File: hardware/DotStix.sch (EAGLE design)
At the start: 22 parts, among them IC1 CAT24M010TS, U1 ATMEGA328P-MU-QFN32, U2 TMP102

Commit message: Add NMOS to minimize leakage through 100uF cap
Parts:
- removed D2: (no value), diode:DIODE-SOD523
- added Q2: BSH103, adafruit:MOSFET-NREFLOW
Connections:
- new net N$5: C6.1, Q2.S
- new net TMP112_VCC: U1.PB6(XTAL1/TOSC1/PCINT6), U2.VCC
- new net VCC_100UF_CAP: Q2.G, U1.PB7(XTAL2/TOSC2/PCINT7)
- net +3V3: now also Q2.D; no longer C6.1, D2.C, U2.VCC
- net GND: no longer D2.A
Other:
- note added: "TMP112 needs VCC from MCU I/O. (reduces draw from 7uA -> ? nA)"
- moved on the sheet: C6, U2
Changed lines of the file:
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@@
 <part name="SUPPLY5" library="supply2" deviceset="GND" device=""/>
 <part name="D1" library="SparkFun" deviceset="SOLAR-IXYS" device="-"/>
-<part name="D2" library="diode" deviceset="DIODE-" device="SOD523"/>
-<part name="SUPPLY8" library="supply2" deviceset="GND" device=""/>
 <part name="D3" library="diode" deviceset="DIODE-" device="SOD523"/>
 <part name="+3V9" library="supply1" deviceset="+3V3" device=""/>
@@
 <part name="U2" library="SparkFun" deviceset="TMP102" device=""/>
 <part name="SUPPLY15" library="supply2" deviceset="GND" device=""/>
-<part name="+3V12" library="supply1" deviceset="+3V3" device=""/>
 <part name="SUPPLY7" library="supply2" deviceset="GND" device=""/>
 <part name="SUPPLY9" library="supply2" deviceset="GND" device=""/>
@@
 <part name="TP5" library="testpad" deviceset="TP" device="TP20SQ"/>
 <part name="TP6" library="testpad" deviceset="TP" device="TP20SQ"/>
+<part name="Q2" library="adafruit" deviceset="MOSFET-N" device="REFLOW" value="BSH103"/>
 </parts>
 <sheets>
@@
 <wire x1="223.52" y1="-5.08" x2="223.52" y2="-86.36" width="0.1524" layer="95" style="longdash"/>
 <text x="167.64" y="-81.28" size="3.81" layer="95">Storage</text>
+<text x="386.08" y="173.99" size="1.27" layer="91">TMP112 needs VCC from MCU I/O. (reduces draw from 7uA -&gt; ? nA)</text>
 </plain>
 <instances>
@@
 <instance part="SUPPLY5" gate="GND" x="76.2" y="53.34"/>
 <instance part="D1" gate="G$1" x="1.27" y="40.64" rot="R270"/>
-<instance part="D2" gate="G$1" x="30.48" y="43.18" rot="R90"/>
-<instance part="SUPPLY8" gate="GND" x="30.48" y="35.56"/>
 <instance part="D3" gate="G$1" x="25.4" y="45.72"/>
 <instance part="+3V9" gate="G$1" x="36.83" y="53.34"/>
@@
 <instance part="R5" gate="G$1" x="78.74" y="71.12" rot="R90"/>
 <instance part="+3V8" gate="G$1" x="78.74" y="78.74"/>
-<instance part="+3V10" gate="G$1" x="276.86" y="162.56"/>
-<instance part="SUPPLY16" gate="GND" x="276.86" y="149.86"/>
-<instance part="C6" gate="G$1" x="276.86" y="157.48"/>
+<instance part="+3V10" gate="G$1" x="297.18" y="180.34"/>
+<instance part="SUPPLY16" gate="GND" x="297.18" y="152.4"/>
+<instance part="C6" gate="G$1" x="297.18" y="160.02"/>
 <instance part="+3V11" gate="G$1" x="97.79" y="156.21"/>
 <instance part="SUPPLY19" gate="GND" x="68.58" y="167.64" rot="R180"/>
@@
 <instance part="RN2" gate="C" x="17.78" y="140.97" rot="R90"/>
 <instance part="RN2" gate="D" x="-10.16" y="140.97" rot="R90"/>
-<instance part="U2" gate="G$1" x="407.67" y="158.75"/>
+<instance part="U2" gate="G$1" x="407.67" y="160.02"/>
 <instance part="SUPPLY15" gate="GND" x="394.97" y="151.13"/>
-<instance part="+3V12" gate="G$1" x="384.81" y="166.37"/>
 <instance part="SUPPLY7" gate="GND" x="417.83" y="151.13"/>
 <instance part="SUPPLY9" gate="GND" x="193.04" y="-50.8"/>
@@
 <instance part="TP5" gate="G$1" x="114.3" y="55.88" rot="R270"/>
 <instance part="TP6" gate="G$1" x="114.3" y="66.04" rot="R270"/>
+<instance part="Q2" gate="G$1" x="294.64" y="170.18"/>
 </instances>
 <busses>
@@
 </segment>
 <segment>
-<pinref part="D2" gate="G$1" pin="A"/>
-<pinref part="SUPPLY8" gate="GND" pin="GND"/>
-<wire x1="30.48" y1="40.64" x2="30.48" y2="38.1" width="0.1524" layer="91"/>
-</segment>
-<segment>
 <pinref part="D1" gate="G$1" pin="C"/>
 <pinref part="SUPPLY10" gate="GND" pin="GND"/>
@@
 <pinref part="U2" gate="G$1" pin="GND"/>
 <pinref part="SUPPLY15" gate="GND" pin="GND"/>
+<wire x1="394.97" y1="154.94" x2="394.97" y2="153.67" width="0.1524" layer="91"/>
 </segment>
 <segment>
 <pinref part="U2" gate="G$1" pin="ADD0"/>
 <pinref part="SUPPLY7" gate="GND" pin="GND"/>
+<wire x1="417.83" y1="154.94" x2="417.83" y2="153.67" width="0.1524" layer="91"/>
 </segment>
 <segment>
@@
 <segment>
 <pinref part="U2" gate="G$1" pin="SDA"/>
-<wire x1="417.83" y1="163.83" x2="420.37" y2="163.83" width="0.1524" layer="91"/>
-<label x="420.37" y="163.83" size="1.27" layer="95" xref="yes"/>
+<wire x1="417.83" y1="165.1" x2="420.37" y2="165.1" width="0.1524" layer="91"/>
+<label x="420.37" y="165.1" size="1.27" layer="95" xref="yes"/>
 </segment>
 <segment>
@@
 <segment>
 <pinref part="D3" gate="G$1" pin="C"/>
-<wire x1="27.94" y1="45.72" x2="30.48" y2="45.72" width="0.1524" layer="91"/>
 <pinref part="+3V9" gate="G$1" pin="+3V3"/>
-<wire x1="30.48" y1="45.72" x2="36.83" y2="45.72" width="0.1524" layer="91"/>
+<wire x1="27.94" y1="45.72" x2="36.83" y2="45.72" width="0.1524" layer="91"/>
 <wire x1="36.83" y1="50.8" x2="36.83" y2="45.72" width="0.1524" layer="91"/>
-<pinref part="D2" gate="G$1" pin="C"/>
-<junction x="30.48" y="45.72"/>
 </segment>
 <segment>
 <pinref part="R5" gate="G$1" pin="2"/>
 <pinref part="+3V8" gate="G$1" pin="+3V3"/>
-</segment>
-<segment>
-<pinref part="+3V10" gate="G$1" pin="+3V3"/>
-<pinref part="C6" gate="G$1" pin="1"/>
 </segment>
 <segment>
@@
 </segment>
 <segment>
-<pinref part="+3V12" gate="G$1" pin="+3V3"/>
-<wire x1="384.81" y1="163.83" x2="394.97" y2="163.83" width="0.1524" layer="91"/>
-<pinref part="U2" gate="G$1" pin="VCC"/>
-</segment>
-<segment>
 <wire x1="193.04" y1="-30.48" x2="193.04" y2="-38.1" width="0.1524" layer="91"/>
 <pinref part="IC1" gate="G$1" pin="VCC"/>
@@
 <pinref part="+3V14" gate="G$1" pin="+3V3"/>
 </segment>
+<segment>
+<pinref part="+3V10" gate="G$1" pin="+3V3"/>
+<pinref part="Q2" gate="G$1" pin="D"/>
+<wire x1="297.18" y1="177.8" x2="297.18" y2="175.26" width="0.1524" layer="91"/>
+</segment>
 </net>
 <net name="MOSI" class="0">
@@
 <segment>
 <pinref part="U2" gate="G$1" pin="SCL"/>
-<wire x1="417.83" y1="161.29" x2="420.37" y2="161.29" width="0.1524" layer="91"/>
-<label x="420.37" y="161.29" size="1.27" layer="95" xref="yes"/>
+<wire x1="417.83" y1="162.56" x2="420.37" y2="162.56" width="0.1524" layer="91"/>
+<label x="420.37" y="162.56" size="1.27" layer="95" xref="yes"/>
 </segment>
 <segment>
@@
 <segment>
 <pinref part="U2" gate="G$1" pin="ALERT"/>
-<wire x1="417.83" y1="156.21" x2="420.37" y2="156.21" width="0.1524" layer="91"/>
-<label x="420.37" y="156.21" size="1.27" layer="95" xref="yes"/>
+<wire x1="417.83" y1="157.48" x2="420.37" y2="157.48" width="0.1524" layer="91"/>
+<label x="420.37" y="157.48" size="1.27" layer="95" xref="yes"/>
 </segment>
 <segment>
@@
 </segment>
 </net>
+<net name="TMP112_VCC" class="0">
+<segment>
+<pinref part="U1" gate="G$1" pin="PB6(XTAL1/TOSC1/PCINT6)"/>
+<wire x1="195.58" y1="68.58" x2="198.12" y2="68.58" width="0.1524" layer="91"/>
+<label x="198.12" y="68.58" size="1.27" layer="95" xref="yes"/>
+</segment>
+<segment>
+<pinref part="U2" gate="G$1" pin="VCC"/>
+<wire x1="394.97" y1="165.1" x2="392.43" y2="165.1" width="0.1524" layer="91"/>
+<label x="392.43" y="165.1" size="1.27" layer="95" rot="R180" xref="yes"/>
+</segment>
+</net>
+<net name="N$5" class="0">
+<segment>
+<pinref part="C6" gate="G$1" pin="1"/>
+<pinref part="Q2" gate="G$1" pin="S"/>
+<wire x1="297.18" y1="165.1" x2="297.18" y2="162.56" width="0.1524" layer="91"/>
+</segment>
+</net>
+<net name="VCC_100UF_CAP" class="0">
+<segment>
+<pinref part="Q2" gate="G$1" pin="G"/>
+<wire x1="292.1" y1="167.64" x2="289.56" y2="167.64" width="0.1524" layer="91"/>
+<label x="289.56" y="167.64" size="1.27" layer="95" rot="R180" xref="yes"/>
+</segment>
+<segment>
+<pinref part="U1" gate="G$1" pin="PB7(XTAL2/TOSC2/PCINT7)"/>
+<wire x1="195.58" y1="63.5" x2="198.12" y2="63.5" width="0.1524" layer="91"/>
+<label x="198.12" y="63.5" size="1.27" layer="95" xref="yes"/>
+</segment>
+</net>

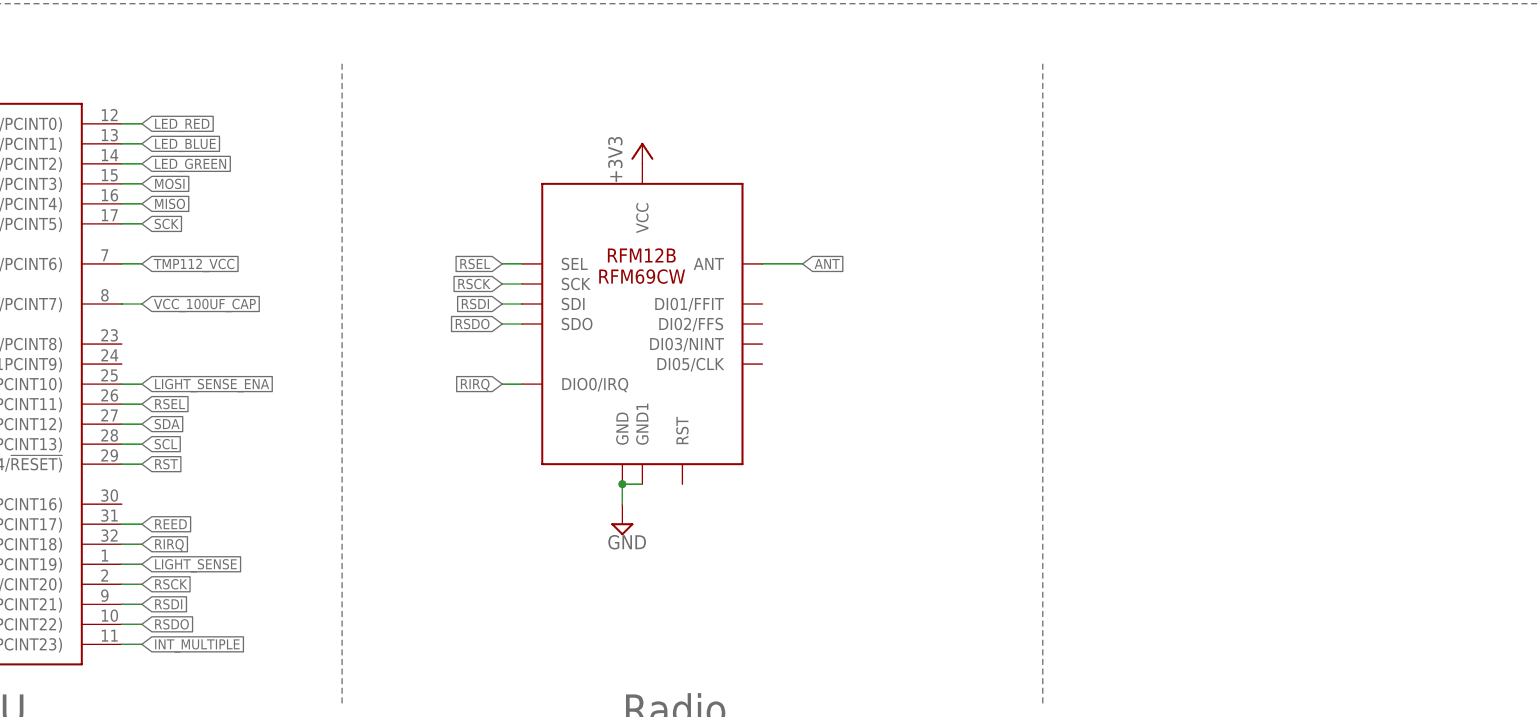
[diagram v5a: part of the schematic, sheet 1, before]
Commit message: Cleanup unused, improve GND
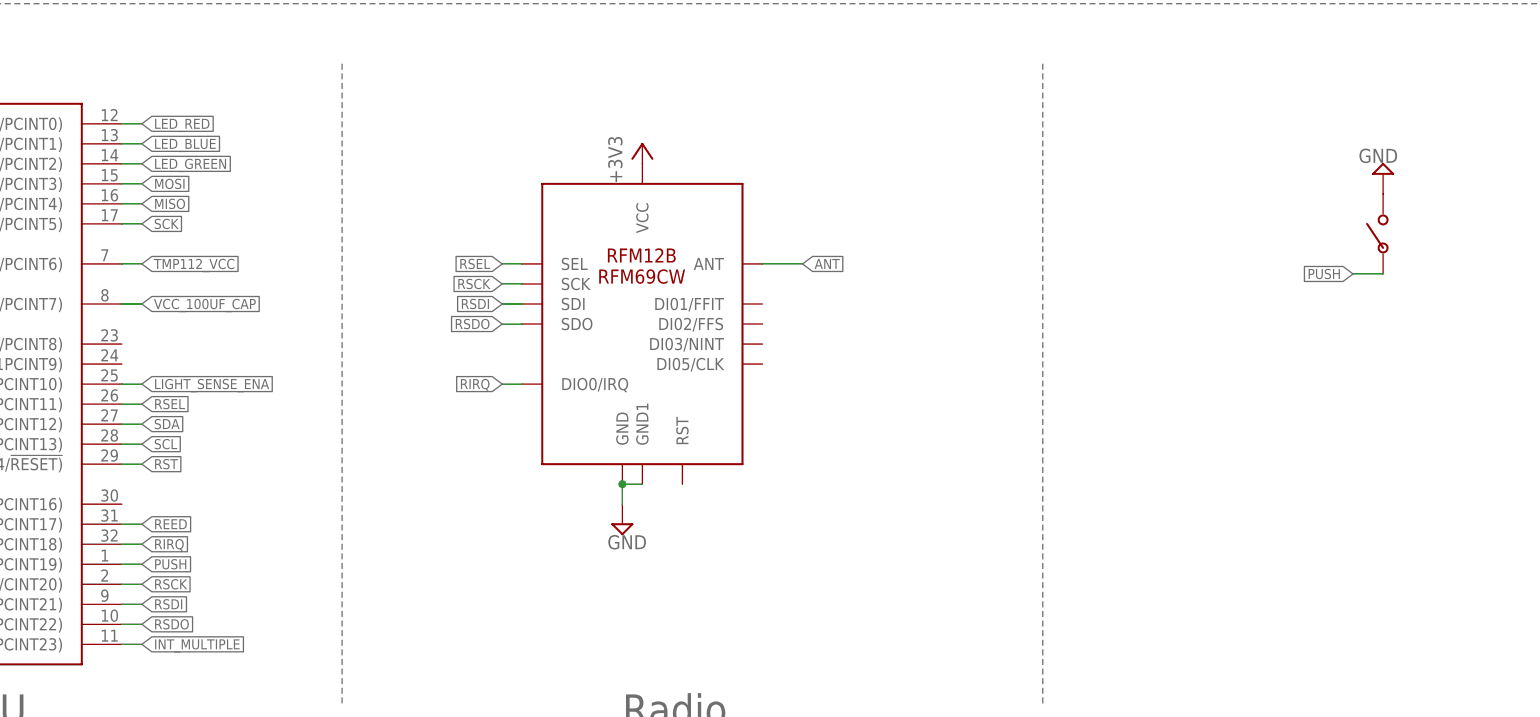
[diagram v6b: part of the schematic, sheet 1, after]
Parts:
- added U$4: PUSHBUTTON_4X2.5, pusbbutton_4x2_5:PUSHBUTTON_4X2.5
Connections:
- removed net LIGHT_SENSE: U1.PD3(INT1/OC2B/PCINT19)
- new net PUSH: U$4.P$1, U1.PD3(INT1/OC2B/PCINT19)
- net GND: now also U$4.P$2
